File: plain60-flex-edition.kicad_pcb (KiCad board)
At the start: 2 copper layers, 284.7 x 94.2 mm, 175 parts, among them J1 HRO-TYPE-C-31-M-12, J2 ISP, J3 ai03_ud, K1 KEYSW, K10 KEYSW, K11 KEYSW, K12 KEYSW, K13 KEYSW, K14 KEYSW, K15 KEYSW, K15-1 KEYSW, K16 KEYSW, K17 KEYSW, K18 KEYSW, K19 KEYSW, K2 KEYSW, K20 KEYSW, K21 KEYSW, K22 KEYSW, K23 KEYSW, K24 KEYSW, K25 KEYSW, K26 KEYSW, K27 KEYSW, K28 KEYSW, K29 KEYSW, K3 KEYSW, K31 KEYSW, K31-1 KEYSW, K32 KEYSW, K33 KEYSW, K34 KEYSW, K35 KEYSW, K36 KEYSW, K37 KEYSW, K38 KEYSW, K39 KEYSW, K4 KEYSW, K40 KEYSW, K41 KEYSW, K42 KEYSW, K43 KEYSW, K44 KEYSW, K44-1 KEYSW, K46 KEYSW, K46-1 KEYSW, K47 KEYSW, K48 KEYSW, K49 KEYSW, K5 KEYSW, K50 KEYSW, K51 KEYSW, K52 KEYSW, K53 KEYSW, K54 KEYSW, K55 KEYSW, K56 KEYSW, K57 KEYSW, K58 KEYSW, K58-1 KEYSW, K59 KEYSW, K6 KEYSW, K61 KEYSW, K61-1 KEYSW, K62 KEYSW, K62-1 KEYSW, K63 KEYSW, K63-1 KEYSW, K67 KEYSW, K67-1 KEYSW, K7 KEYSW, K71 KEYSW, K72 KEYSW, K72-1 KEYSW, K73 KEYSW, K73-1 KEYSW, K74 KEYSW, K74-1 KEYSW, K8 KEYSW, K9 KEYSW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

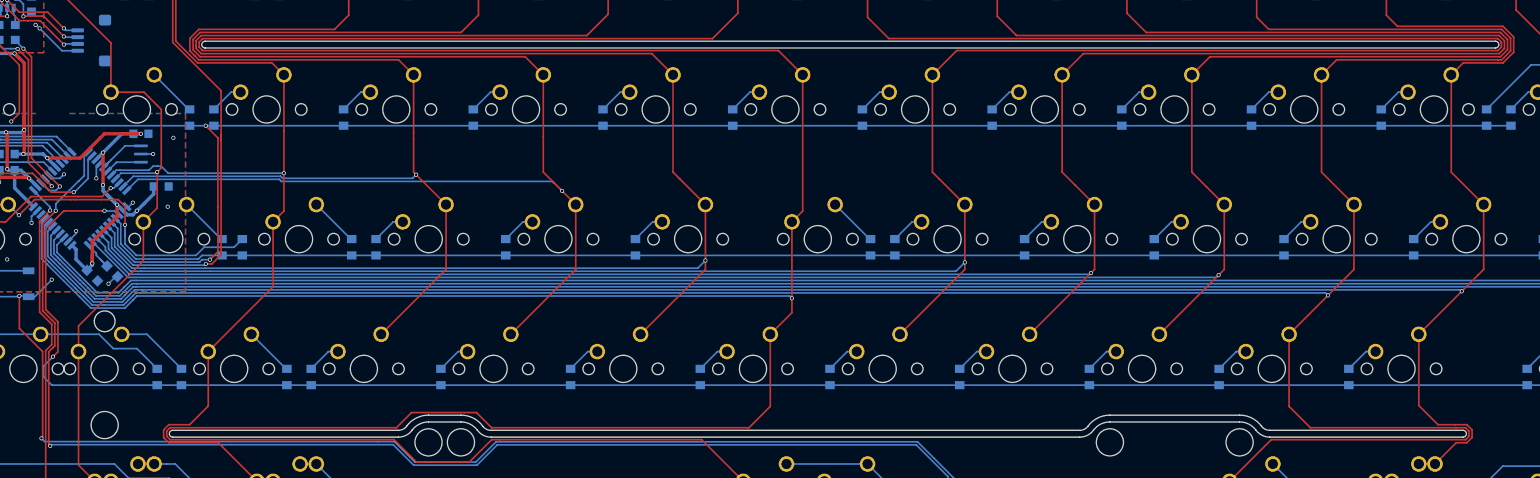
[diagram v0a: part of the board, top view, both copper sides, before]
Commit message: removed flex cuts and renamed to Thin Edition
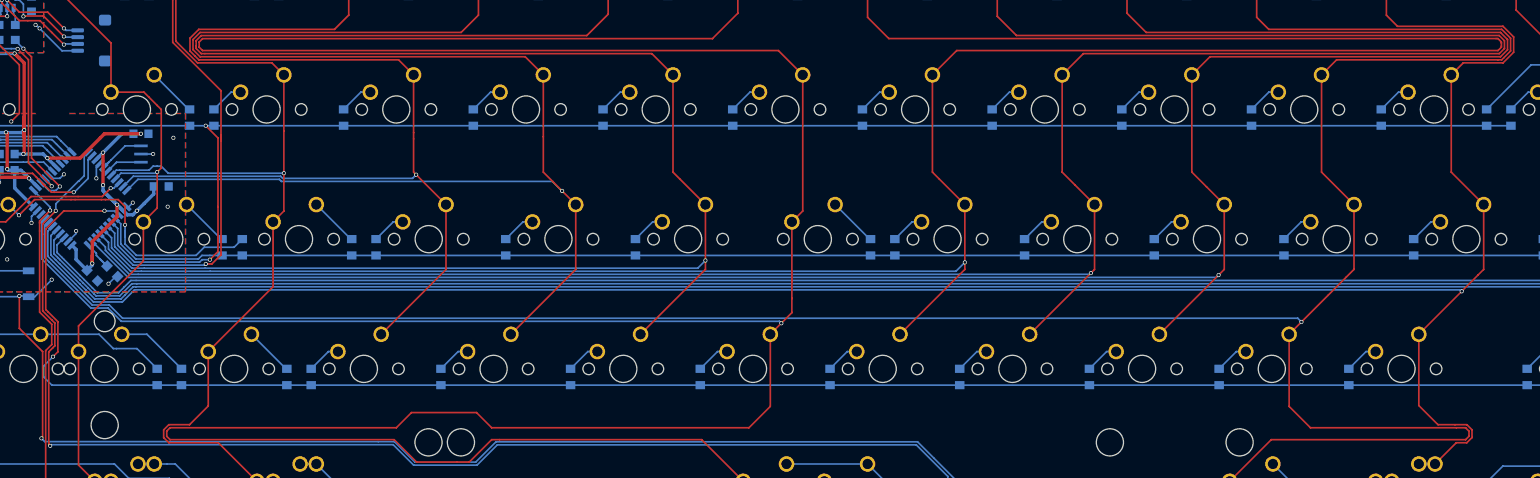
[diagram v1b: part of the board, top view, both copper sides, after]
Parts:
- removed G***: LOGO, footprints:oshw
- removed G***: LOGO, Keeb_components:logo_new
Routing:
- net col10: track 399.1 -> 395.4 mm
- net col6: track 547.6 -> 546.1 mm
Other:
- outline, holes or cut-outs redrawn
- board text added: "Plain60 Thin Edition"
- board text added: "based on Plain60 Flex Edition rev2.2"
- board text removed: "Plain60 Flex Edition"
- board text removed: "based on Plain60 rev2.2"
